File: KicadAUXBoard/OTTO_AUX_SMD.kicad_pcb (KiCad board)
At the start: 2 copper layers, 288.5 x 95 mm, 212 parts, among them J1 Conn_01x12, J1_KD028QVFMA17 Conn_02x25_Counter_Clockwise, Q1 AO3400A, SW1 ALPS SKHC, SW10 ALPS SKHC, SW11 ALPS SKHC, SW12 ALPS SKHC, SW13 ALPS SKHC, SW14 ALPS SKHC, SW15 ALPS SKHC, SW16 ALPS SKHC, SW17 ALPS SKHC, SW18 ALPS SKHC, SW19 ALPS SKHC, SW2 ALPS SKHC, SW20 ALPS SKHC, SW21 ALPS SKHC, SW22 ALPS SKHC, SW23 ALPS SKHC, SW24 ALPS SKHC, SW25 ALPS SKHC, SW26 ALPS SKHC, SW27 6x6x13mm, SW28 6x6x13mm, SW29 6x6x13mm, SW3 ALPS SKHC, SW30 6x6x13mm, SW31 6x6x13mm, SW32 6x6x13mm, SW33 6x6x13mm, SW34 6x6x13mm, SW35 6x6x13mm, SW36 6x6x13mm, SW37 6x6x13mm, SW38 6x6x13mm, SW39 6x6x13mm, SW4 ALPS SKHC, SW40 6x6x13mm, SW41 6x6x13mm, SW42 6x6x13mm, SW43 6x6x13mm, SW44 6x6x13mm, SW45 6x6x13mm, SW46 6x6x13mm, SW47 6x6x13mm, SW5 ALPS SKHC, SW50 6x6x13mm, SW51 6x6x13mm, SW52 6x6x13mm, SW53 6x6x13mm, SW54 6x6x13mm, SW55 6x6x13mm, SW56 6x6x13mm, SW6 ALPS SKHC, SW7 ALPS SKHC, SW8 ALPS SKHC, SW9 ALPS SKHC, U1 SN74LV1T34_SOT-23_A, U2 TPS22918_SOT23-6_A

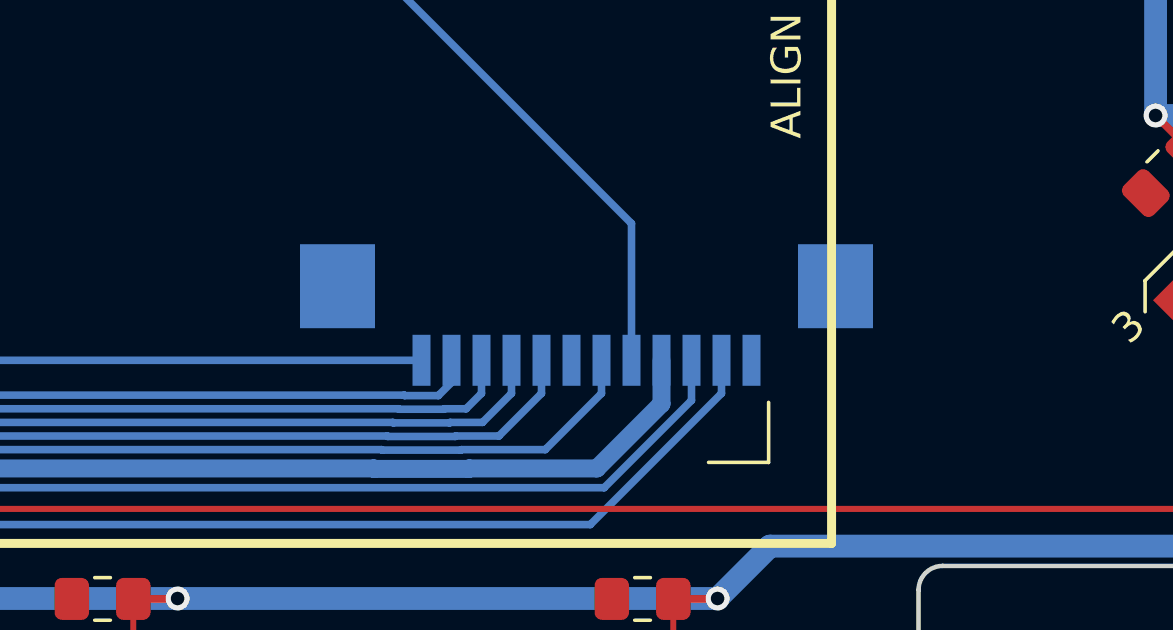
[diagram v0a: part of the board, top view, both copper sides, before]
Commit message: WIP: FPC connector, increase number of lanes. Main board routed
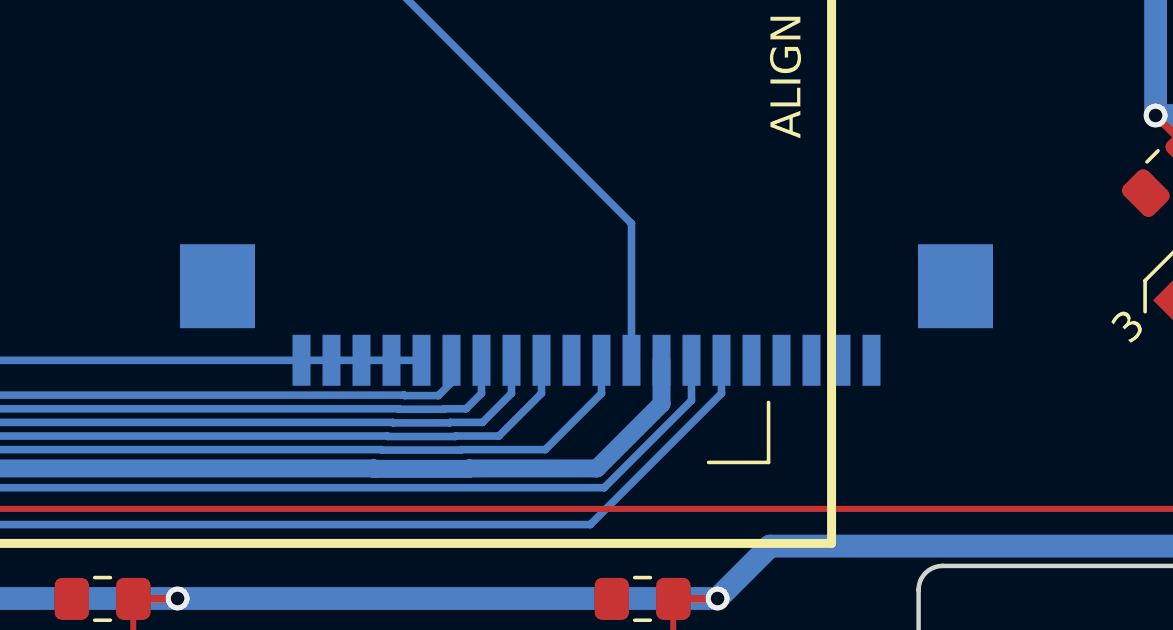
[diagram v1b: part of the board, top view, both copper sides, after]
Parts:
- J1: value Conn_01x12 -> Conn_01x20; footprint OTTO_Footprints_Lib:X10B25L12T_FPC_1x12-1MP_P1.00mm_Horizontal -> OTTO_Footprints_Lib:X10B25L20T_FPC_1x20-1MP_P1.00mm_Horizontal
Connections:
- J1 pad 10: /SPI_MOSI_MCU -> SPI_CS_RASPI
- J1 pad 11: LED_PWR_EN -> RESET
- J1 pad 2: 3V3 -> 5V_BACKLIGHT
- J1 pad 3: SPI_MOSI_RASPI -> 5V_BACKLIGHT
- J1 pad 4: SPI_SCLK_RASPI -> 3V3
- J1 pad 5: SPI_CS_RASPI -> 3V3
- J1 pad 6: GND -> 3V3
- J1 pad 7: RESET -> SPI_MOSI_RASPI
- J1 pad 8: BL_PWM -> SPI_SCLK_RASPI
- J1 pad 9: +5V_REG -> GND

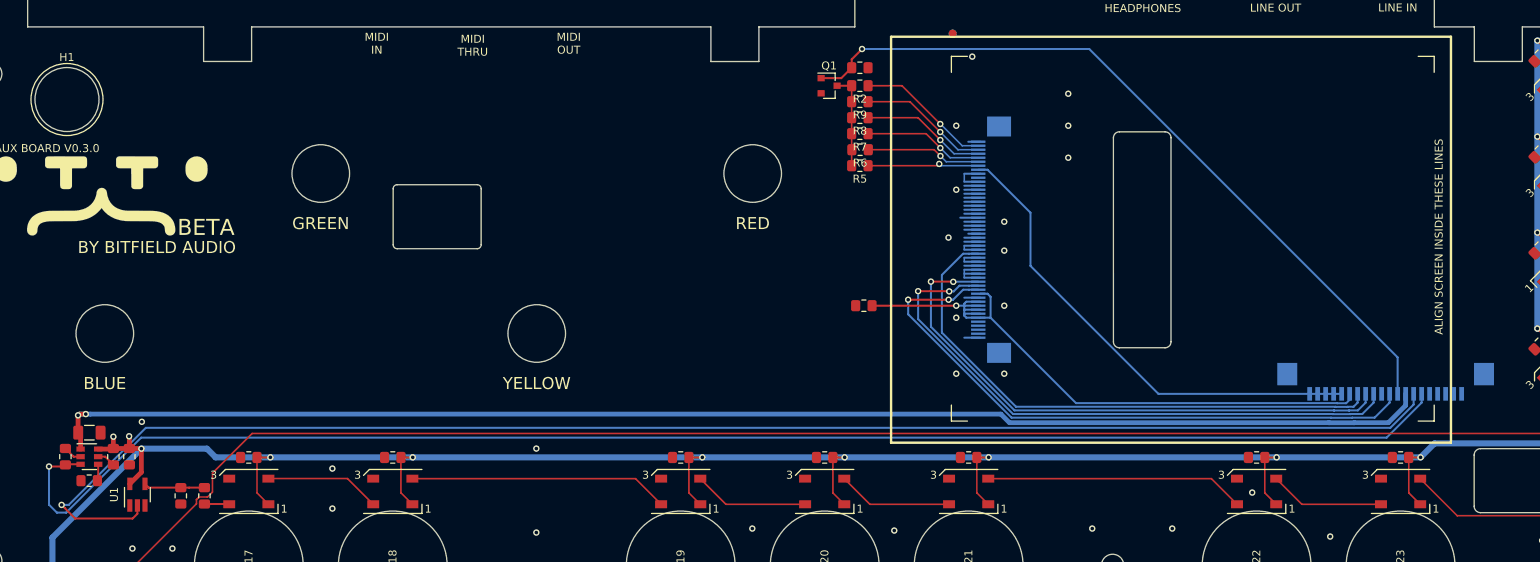
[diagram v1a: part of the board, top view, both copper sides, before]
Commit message: FPC connector, increase number of lanes. AUX board routed
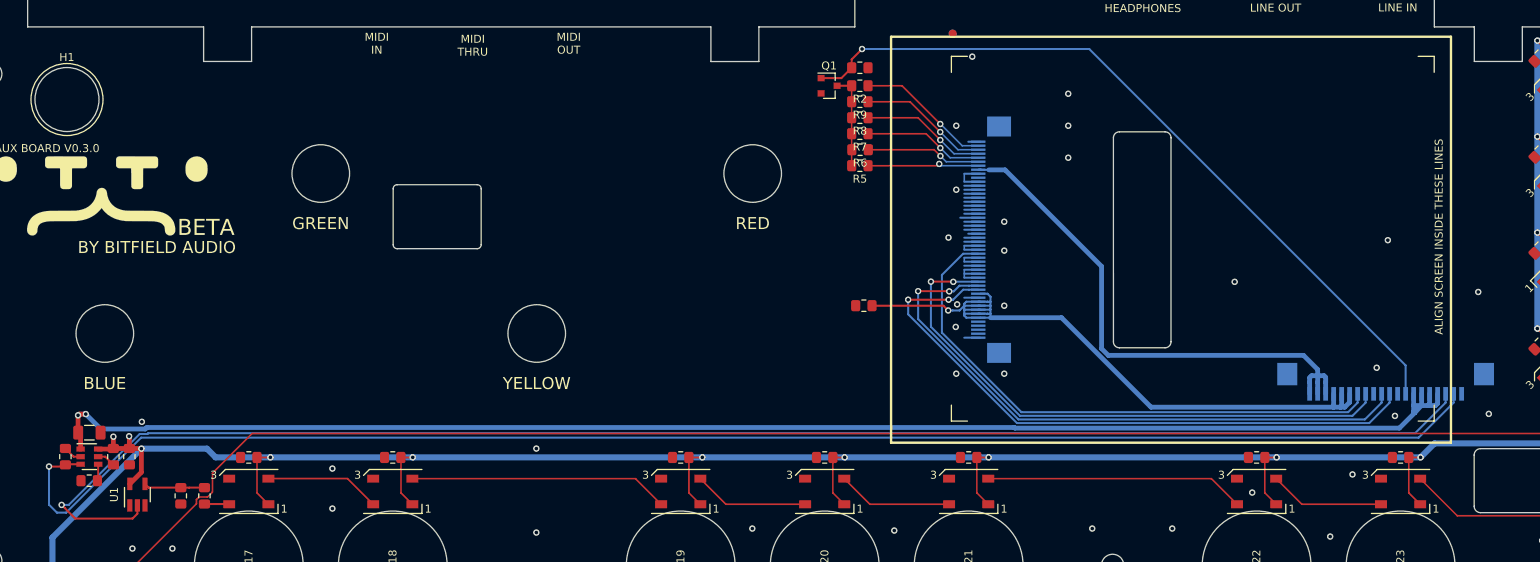
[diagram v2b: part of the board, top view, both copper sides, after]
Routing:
- net 3V3: track 78.8 -> 90.2 mm
- net +5V_REG: track 174.2 -> 185.2 mm
- net 5V_BACKLIGHT: track 60.9 -> 68.5 mm
- net LED_PWR_EN: track 187.7 -> 191.7 mm
- net /SPI_MOSI_MCU: track 187.0 -> 190.9 mm
- net SPI_CS_RASPI: track 74.9 -> 76.4 mm
- net RESET: track 78.5 -> 79.1 mm
- net SPI_SCLK_RASPI: track 71.8 -> 72.3 mm
- net SPI_MOSI_RASPI: track 70.0 -> 70.6 mm
- net GND: vias 30 -> 38

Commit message: Fix board connection FPC connector rotation
Also includes:
 - Slight cleanup of routing on both boards
 - Smaller holes for screws on aux board
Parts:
- moved U1 1.78 mm to (41.1, 71.8)
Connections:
- J1 pad 1: 5V_BACKLIGHT -> GND
- J1 pad 10: SPI_CS_RASPI -> 3V3
- J1 pad 11: RESET -> 3V3
- J1 pad 12: GND -> RESET
- J1 pad 13: BL_PWM -> SPI_CS_RASPI
- J1 pad 14: +5V_REG -> GND
- J1 pad 15: +5V_REG -> SPI_SCLK_RASPI
- J1 pad 16: +5V_REG -> SPI_MOSI_RASPI
- J1 pad 17: +5V_REG -> GND
- J1 pad 18: /SPI_MOSI_MCU -> 5V_BACKLIGHT
- J1 pad 19: LED_PWR_EN -> 5V_BACKLIGHT
- J1 pad 2: 5V_BACKLIGHT -> LED_PWR_EN
- J1 pad 20: GND -> 5V_BACKLIGHT
- J1 pad 3: 5V_BACKLIGHT -> /SPI_MOSI_MCU
- J1 pad 4: 3V3 -> GND
- J1 pad 5: 3V3 -> +5V_REG
- J1 pad 6: 3V3 -> +5V_REG
- J1 pad 7: SPI_MOSI_RASPI -> +5V_REG
- J1 pad 8: SPI_SCLK_RASPI -> BL_PWM
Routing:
- net GND: track 64.6 -> 102.7 mm, vias 38 -> 119
- net /SPI_MOSI_MCU: track 190.9 -> 156.3 mm
- net LED_PWR_EN: track 191.7 -> 168.8 mm
- net RESET: track 79.1 -> 61.2 mm, vias 2 -> 0
- net 5V_BACKLIGHT: track 68.5 -> 83.2 mm
- net +5V_REG: track 185.2 -> 170.8 mm
- net SPI_CS_RASPI: track 76.4 -> 62.4 mm, vias 2 -> 0
- net SPI_SCLK_RASPI: track 72.3 -> 64.3 mm, vias 2 -> 0
- net BL_PWM: track 95.1 -> 90.2 mm
- net 3V3: track 90.2 -> 94.7 mm
- net Net-(LED8-Pad2): track 14.8 -> 18.7 mm
- net SPI_MOSI_RASPI: track 70.6 -> 66.8 mm
- net Net-(J1_KD028QVFMA17-Pad47): track 15.9 -> 18.2 mm
- net Net-(J1_KD028QVFMA17-Pad48): track 16.5 -> 18.5 mm
- net Net-(J1_KD028QVFMA17-Pad46): track 15.3 -> 17.3 mm
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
